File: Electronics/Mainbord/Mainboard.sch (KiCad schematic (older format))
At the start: 42 parts, among them J1 Raspberry_Pi_2_3, J2 Screw_Terminal_01x03, J3 Screw_Terminal_01x03, J4 Screw_Terminal_01x03, J5 Screw_Terminal_01x03, J6 Screw_Terminal_01x03, J7 Screw_Terminal_01x03, J8 Screw_Terminal_01x03, J9 Screw_Terminal_01x03, U1 ESP32-WROOM-32, U6 74HC4051, U7 LD1117V33, U8 74HC595

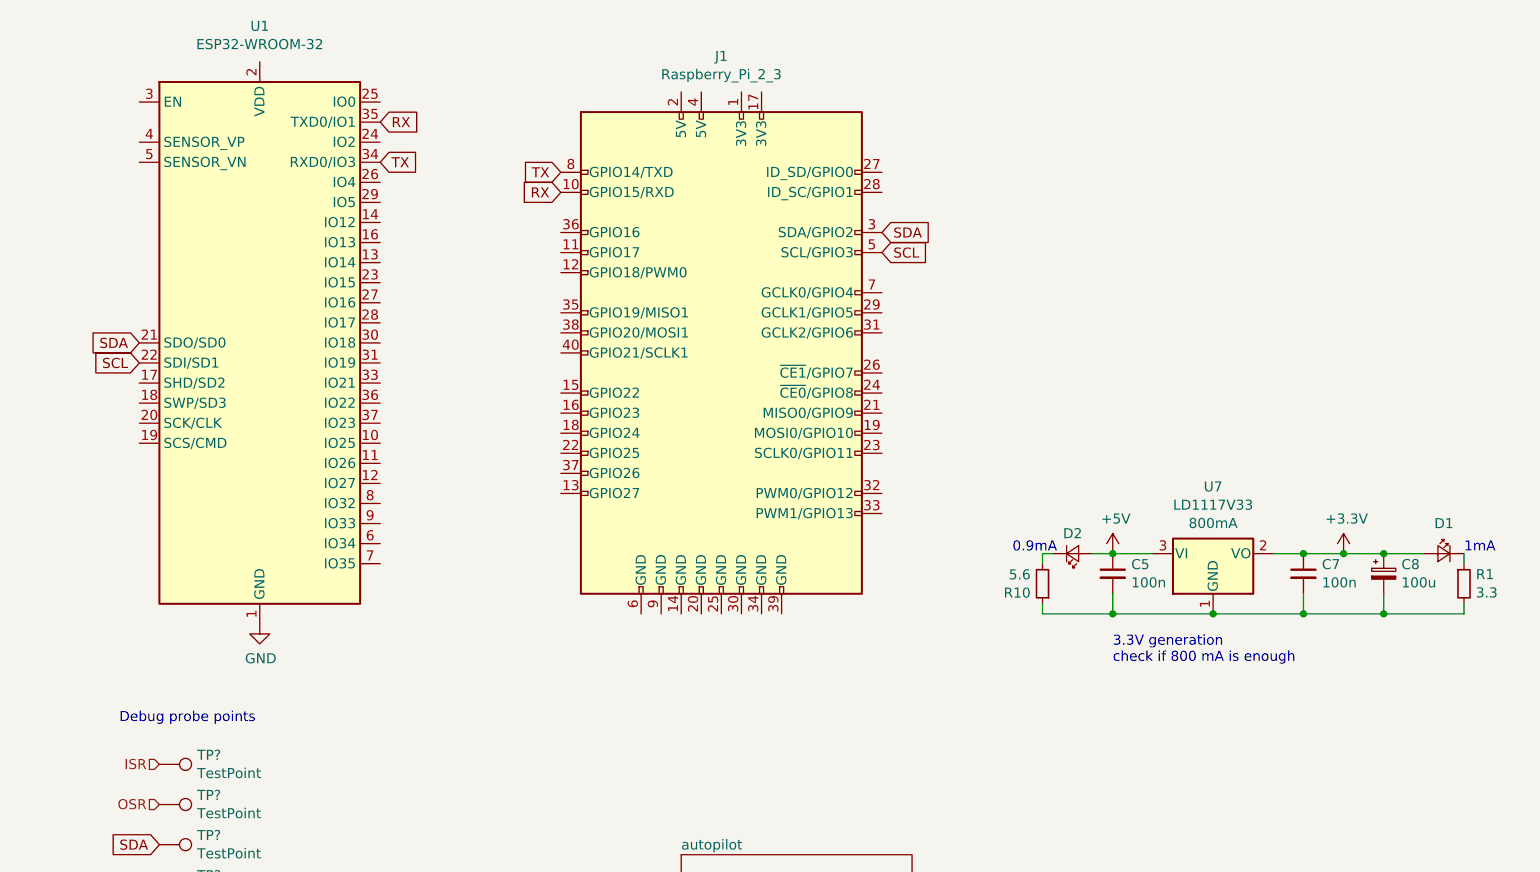
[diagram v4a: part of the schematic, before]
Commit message: Electronics - Replaced ESP32 library
The previous ESP32 library esp32_dev_kit was
not providing a footprint and schema corresponding to
the devkit module.
I have added the library ESP32-DEVKITC-32D from snapeda.com

I have also updated the footprint for the Raspberry pi.
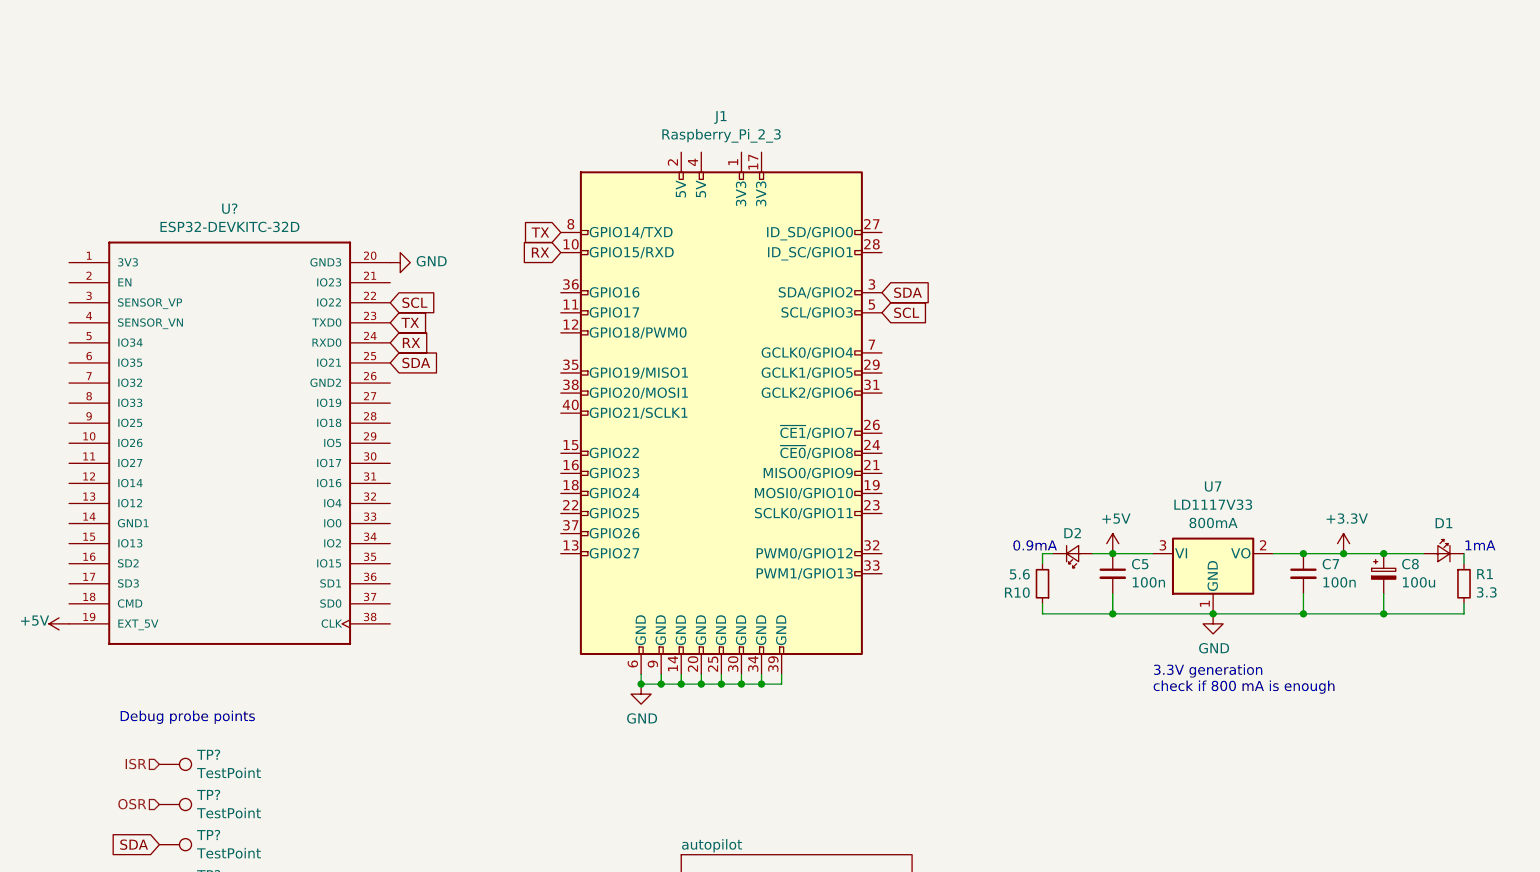
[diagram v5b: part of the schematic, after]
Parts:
- removed U1: ESP32-WROOM-32, RF_Module:ESP32-WROOM-32, symbol RF_Module:ESP32-WROOM-32
- added U?: ESP32-DEVKITC-32D, MODULE_ESP32-DEVKITC-32D, symbol ESP32-DEVKITC-32D:ESP32-DEVKITC-32D
- J1: footprint (none) -> Connector_PinHeader_2.54mm:PinHeader_2x14_P2.54mm_Vertical
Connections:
- net +5V: now also U?.19 (EXT_5V)
- net GND: now also C5.2, C7.2, C8.2, J1.14 (GND), J1.20 (GND), J1.25 (GND), J1.30 (GND), J1.34 (GND), J1.39 (GND), J1.6 (GND), J1.9 (GND), R1.2, R10.1, U7.1 (GND), U?.20 (GND3)
- net RX: now also U?.24 (RXD0)
- net SCL: now also U?.22 (IO22)
- net SDA: now also U?.25 (IO21)
- net TX: now also U?.23 (TXD0)
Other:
- moved on the sheet: J1
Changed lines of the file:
@@
 $EndDescr
 $Comp
-L RF_Module:ESP32-WROOM-32 U1
-U 1 1 5DB57404
-P 1700 2500
-F 0 "U1" H 1700 4078 50  0000 C CNN
-F 1 "ESP32-WROOM-32" H 1700 3987 50  0000 C CNN
-F 2 "RF_Module:ESP32-WROOM-32" H 1700 1000 50  0001 C CNN
-F 3 "https://www.espressif.com/sites/default/files/documentation/esp32-wroom-32_datasheet_en.pdf" H 1400 2550 50  0001 C CNN
-	1    1700 2500
-	1    0    0    -1
-$EndComp
-$Comp
 L Connector:Raspberry_Pi_2_3 J1
 U 1 1 5DB57867
-P 4000 2550
-F 0 "J1" H 4000 4028 50  0000 C CNN
-F 1 "Raspberry_Pi_2_3" H 4000 3937 50  0000 C CNN
-F 2 "" H 4000 2550 50  0001 C CNN
-F 3 "https://www.raspberrypi.org/documentation/hardware/raspberrypi/schematics/rpi_SCH_3bplus_1p0_reduced.pdf" H 4000 2550 50  0001 C CNN
-	1    4000 2550
+P 4000 2850
+F 0 "J1" H 4000 4328 50  0000 C CNN
+F 1 "Raspberry_Pi_2_3" H 4000 4237 50  0000 C CNN
+F 2 "Connector_PinHeader_2.54mm:PinHeader_2x14_P2.54mm_Vertical" H 4000 2850 50  0001 C CNN
+F 3 "https://www.raspberrypi.org/documentation/hardware/raspberrypi/schematics/rpi_SCH_3bplus_1p0_reduced.pdf" H 4000 2850 50  0001 C CNN
+	1    4000 2850
 	1    0    0    -1
 $EndComp
@@
 Wire Wire Line
 	7100 3550 7300 3550
-Text Notes 5950 4100 0    50   ~ 0
+Text Notes 6150 4250 0    50   ~ 0
 3.3V generation\ncheck if 800 mA is enough
-Text GLabel 3200 1650 0    50   Input ~ 0
+Text GLabel 3200 1950 0    50   Input ~ 0
 TX
-Text GLabel 3200 1750 0    50   Input ~ 0
+Text GLabel 3200 2050 0    50   Input ~ 0
 RX
-Text GLabel 2300 1600 2    50   Input ~ 0
-TX
-Text GLabel 2300 1400 2    50   Input ~ 0
-RX
-Text GLabel 4800 1950 2    50   Input ~ 0
-SDA
-Text GLabel 4800 2050 2    50   Input ~ 0
-SCL
-$Comp
-L power:GND #PWR?
-U 1 1 5DBAD619
-P 1700 3900
-AR Path="/5DB6029E/5DBAD619" Ref="#PWR?"  Part="1"
-AR Path="/5DBAD619" Ref="#PWR0176"  Part="1"
-F 0 "#PWR0176" H 1700 3650 50  0001 C CNN
-F 1 "GND" H 1705 3727 50  0000 C CNN
-F 2 "" H 1700 3900 50  0001 C CNN
-F 3 "" H 1700 3900 50  0001 C CNN
-	1    1700 3900
-	1    0    0    -1
-$EndComp
-Text GLabel 1100 2500 0    50   Input ~ 0
+Text GLabel 4800 2250 2    50   Input ~ 0
 SDA
-Text GLabel 1100 2600 0    50   Input ~ 0
+Text GLabel 4800 2350 2    50   Input ~ 0
 SCL
 Text Label 9300 1900 2    50   ~ 0
@@
 	6050 6350 6700 6350
 $Bitmap
-Pos 13700 2050
+Pos 1400 800
 Scale 1.000000
 Data
@@
 	0    1    1    0
 $EndComp
+$Comp
+L ESP32-DEVKITC-32D:ESP32-DEVKITC-32D U?
+U 1 1 5DF7E5CE
+P 1550 3000
+F 0 "U?" H 1550 4167 50  0000 C CNN
+F 1 "ESP32-DEVKITC-32D" H 1550 4076 50  0000 C CNN
+F 2 "MODULE_ESP32-DEVKITC-32D" H 1550 3000 50  0001 L BNN
+F 3 "ESP32-DEVKITC-32D" H 1550 3000 50  0001 L BNN
+F 4 "None" H 1550 3000 50  0001 L BNN "Field4"
+F 5 "Espressif Systems" H 1550 3000 50  0001 L BNN "Field5"
+F 6 "None" H 1550 3000 50  0001 L BNN "Field6"
+F 7 "EVAL BOARD FOR ESP-WROOM-32" H 1550 3000 50  0001 L BNN "Field7"
+F 8 "Unavailable" H 1550 3000 50  0001 L BNN "Field8"
+	1    1550 3000
+	1    0    0    -1
+$EndComp
+Text GLabel 2350 2300 2    50   Input ~ 0
+SCL
+Text GLabel 2350 2600 2    50   Input ~ 0
+SDA
+Text GLabel 2350 2400 2    50   Input ~ 0
+TX
+Text GLabel 2350 2500 2    50   Input ~ 0
+RX
+$Comp
+L power:+5V #PWR?
+U 1 1 5DF8EA94
+P 750 3900
+F 0 "#PWR?" H 750 3750 50  0001 C CNN
+F 1 "+5V" V 765 4073 50  0000 C CNN
+F 2 "" H 750 3900 50  0001 C CNN
+F 3 "" H 750 3900 50  0001 C CNN
+	1    750  3900
+	0    -1   -1   0
+$EndComp
+$Comp
+L power:GND #PWR?
+U 1 1 5DF9235F
+P 6450 3850
+F 0 "#PWR?" H 6450 3600 50  0001 C CNN
+F 1 "GND" H 6455 3677 50  0000 C CNN
+F 2 "" H 6450 3850 50  0001 C CNN
+F 3 "" H 6450 3850 50  0001 C CNN
+	1    6450 3850
+	1    0    0    -1
+$EndComp
+$Comp
+L power:GND #PWR?
+U 1 1 5DF923C5
+P 2350 2100
+F 0 "#PWR?" H 2350 1850 50  0001 C CNN
+F 1 "GND" V 2355 1972 50  0000 R CNN
+F 2 "" H 2350 2100 50  0001 C CNN
+F 3 "" H 2350 2100 50  0001 C CNN
+	1    2350 2100
+	0    -1   -1   0
+$EndComp
+Wire Wire Line
+	3600 4150 3600 4200
+Wire Wire Line
+	3600 4200 3700 4200
+Wire Wire Line
+	3700 4200 3700 4150
+Wire Wire Line
+	3700 4200 3800 4200
+Wire Wire Line
+	3800 4200 3800 4150
+Connection ~ 3700 4200
+Wire Wire Line
+	3800 4200 3900 4200
+Wire Wire Line
+	3900 4200 3900 4150
+Connection ~ 3800 4200
+Wire Wire Line
+	3900 4200 4000 4200
+Wire Wire Line
+	4000 4200 4000 4150
+Connection ~ 3900 4200
+Wire Wire Line
+	4000 4200 4100 4200
+Wire Wire Line
+	4100 4200 4100 4150
+Connection ~ 4000 4200
+Wire Wire Line
+	4100 4200 4200 4200
+Wire Wire Line
+	4200 4200 4200 4150
+Connection ~ 4100 4200
+Wire Wire Line
+	4200 4200 4300 4200
+Wire Wire Line
+	4300 4200 4300 4150
+Connection ~ 4200 4200
+$Comp
+L power:GND #PWR?
+U 1 1 5DFBA645
+P 3600 4200
+F 0 "#PWR?" H 3600 3950 50  0001 C CNN
+F 1 "GND" H 3605 4027 50  0000 C CNN
+F 2 "" H 3600 4200 50  0001 C CNN
+F 3 "" H 3600 4200 50  0001 C CNN
+	1    3600 4200
+	1    0    0    -1
+$EndComp
+Connection ~ 3600 4200
 $EndSCHEMATC
